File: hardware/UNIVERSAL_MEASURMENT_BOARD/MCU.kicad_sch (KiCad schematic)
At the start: 14 parts, among them U1 STM32G484RET3, U2 ADS8863IDGS, Y1 ATX-H11-F-16.000MHz-G100-T

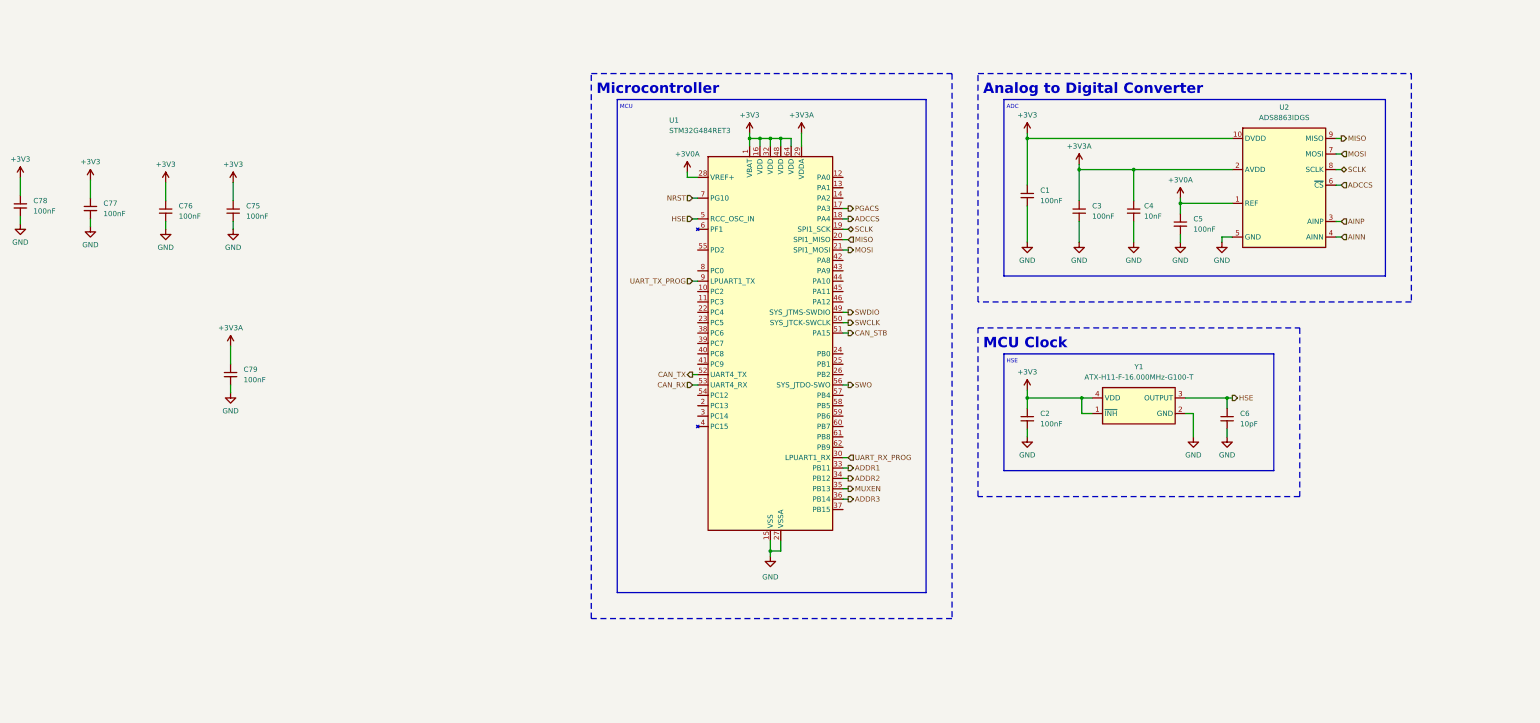
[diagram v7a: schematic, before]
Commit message: Solved ERC problems
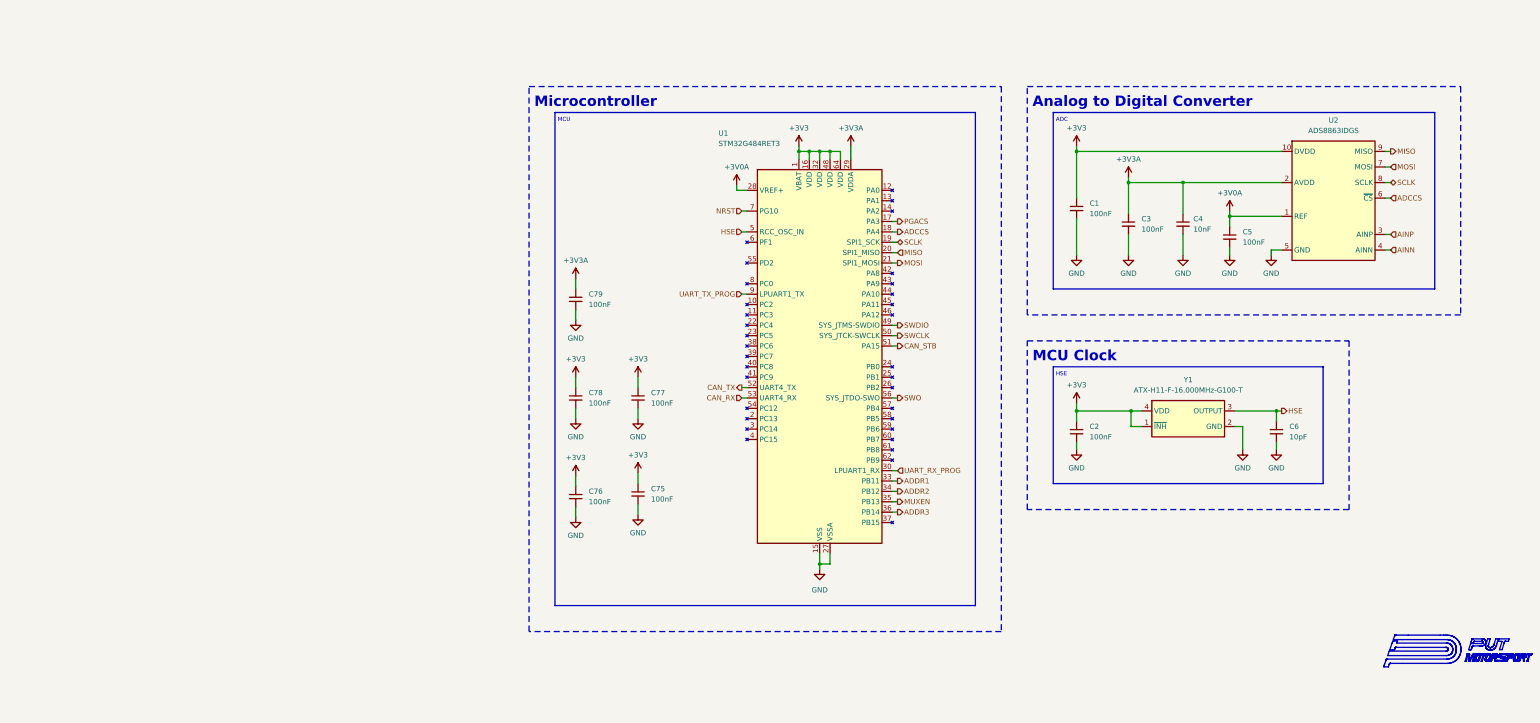
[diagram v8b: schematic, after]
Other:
- moved on the sheet: C1, C2, C3, C4, C5, C6, C75, C76, C77, C78, C79, U2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
